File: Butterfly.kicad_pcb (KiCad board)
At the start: 2 copper layers, 93.1 x 65.5 mm, 28 parts, among them J1 Conn_02x03_Odd_Even, J2 USB_A, U1 ATTINY85-20PU

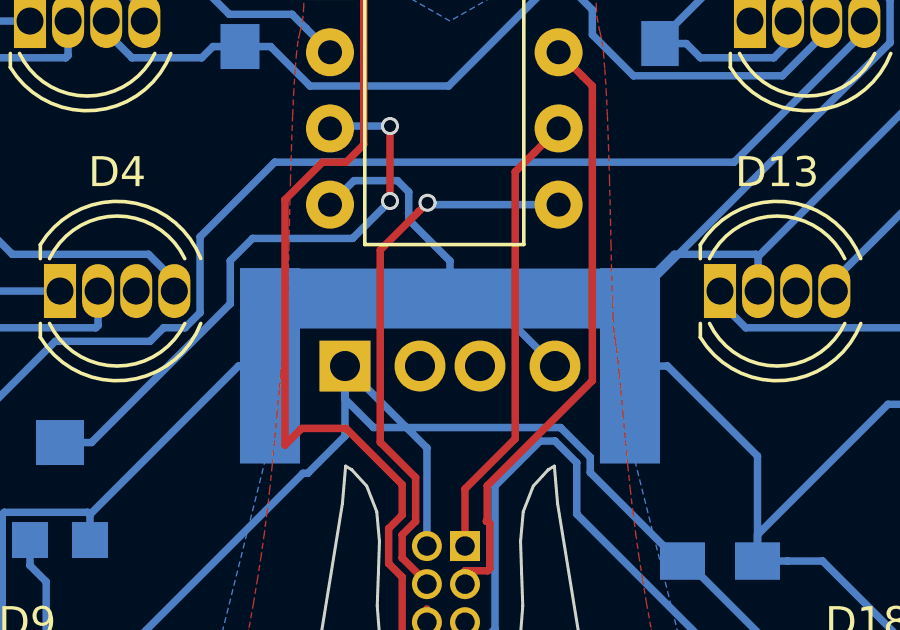
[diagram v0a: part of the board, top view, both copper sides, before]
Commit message: Fill zones.
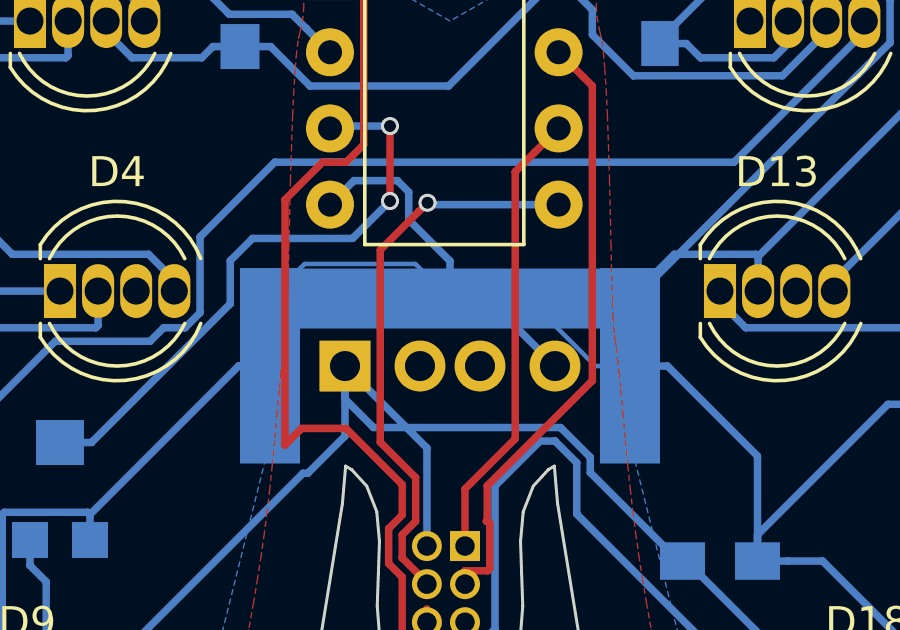
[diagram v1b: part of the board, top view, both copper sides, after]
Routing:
- net GND: track 407.0 -> 423.2 mm
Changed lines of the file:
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@@
   (general
     (links 75)
-    (no_connects 16)
+    (no_connects 0)
     (area 98.409153 69.322099 191.590847 134.925641)
     (thickness 1.6)
     (drawings 182)
-    (tracks 337)
+    (tracks 344)
     (zones 0)
     (modules 28)
@@
   (segment (start 152 93.25) (end 148.87 93.25) (width 0.25) (layer B.Cu) (net 1))
   (segment (start 148.87 93.25) (end 148.62 93.5) (width 0.25) (layer B.Cu) (net 1))
+  (segment (start 145 104.25) (end 147.5976 104.25) (width 0.1524) (layer B.Cu) (net 2))
+  (segment (start 147.5976 104.25) (end 149.8476 106.5) (width 0.1524) (layer B.Cu) (net 2))
+  (segment (start 149.8476 106.5) (end 151 106.5) (width 0.1524) (layer B.Cu) (net 2))
+  (segment (start 139 106.5) (end 139 104.25) (width 0.1524) (layer B.Cu) (net 2))
+  (segment (start 139 104.25) (end 140.1524 103.0976) (width 0.1524) (layer B.Cu) (net 2))
+  (segment (start 143.8476 103.0976) (end 145 104.25) (width 0.1524) (layer B.Cu) (net 2))
+  (segment (start 140.1524 103.0976) (end 143.8476 103.0976) (width 0.1524) (layer B.Cu) (net 2))
   (segment (start 130.27 119) (end 130.27 117.85) (width 0.25) (layer B.Cu) (net 2))
   (segment (start 130.27 117.85) (end 130.074999 117.654999) (width 0.25) (layer B.Cu) (net 2))
@@
     (connect_pads (clearance 0.508))
     (min_thickness 0.254)
-    (fill (arc_segments 16) (thermal_gap 0.508) (thermal_bridge_width 0.508))
+    (fill yes (arc_segments 16) (thermal_gap 0.508) (thermal_bridge_width 0.508))
     (polygon
       (pts
@@
         (xy 101.159481 75.389431) (xy 101.268235 74.91297) (xy 101.448595 74.425842) (xy 101.611785 74.073037) (xy 102.058151 73.335693)
         (xy 102.610262 72.72205) (xy 103.258173 72.24239) (xy 103.51812 72.10195) (xy 103.815052 71.962921) (xy 104.052406 71.87908)
-        (xy 104.292884 71.837641) (xy 104.599189 71.825822) (xy 104.86207 71.82795)
+        (xy 104.292884 71.837641) (xy 104.599189 71.825822)
       )
     )
@@
     (connect_pads (clearance 0.508))
     (min_thickness 0.254)
-    (fill (arc_segments 16) (thermal_gap 0.508) (thermal_bridge_width 0.508))
+    (fill yes (arc_segments 16) (thermal_gap 0.508) (thermal_bridge_width 0.508))
     (polygon
       (pts
@@
         (xy 188.840519 75.389431) (xy 188.731765 74.91297) (xy 188.551405 74.425842) (xy 188.388215 74.073037) (xy 187.941849 73.335693)
         (xy 187.389738 72.72205) (xy 186.741827 72.24239) (xy 186.48188 72.10195) (xy 186.184948 71.962921) (xy 185.947594 71.87908)
-        (xy 185.707116 71.837641) (xy 185.400811 71.825822) (xy 185.13793 71.82795)
+        (xy 185.707116 71.837641) (xy 185.400811 71.825822)
       )
     )
@@
     (connect_pads (clearance 0.508))
     (min_thickness 0.254)
-    (fill (arc_segments 16) (thermal_gap 0.508) (thermal_bridge_width 0.508))
+    (fill yes (arc_segments 16) (thermal_gap 0.508) (thermal_bridge_width 0.508))
     (polygon
       (pts
         (xy 145 95) (xy 110 75) (xy 105 90) (xy 120 105) (xy 120 125)
         (xy 135 125) (xy 140 105) (xy 150 105) (xy 155 125) (xy 170 125)
-        (xy 170 105) (xy 185 90) (xy 180 75) (xy 145 95)
+        (xy 170 105) (xy 185 90) (xy 180 75)
       )
     )

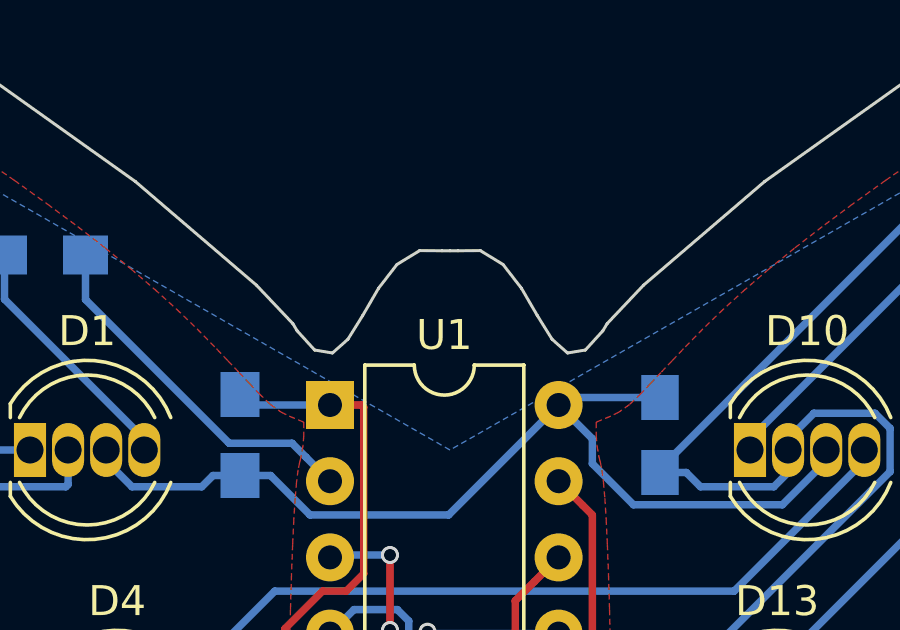
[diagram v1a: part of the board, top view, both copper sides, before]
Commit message: Add antenna holes.
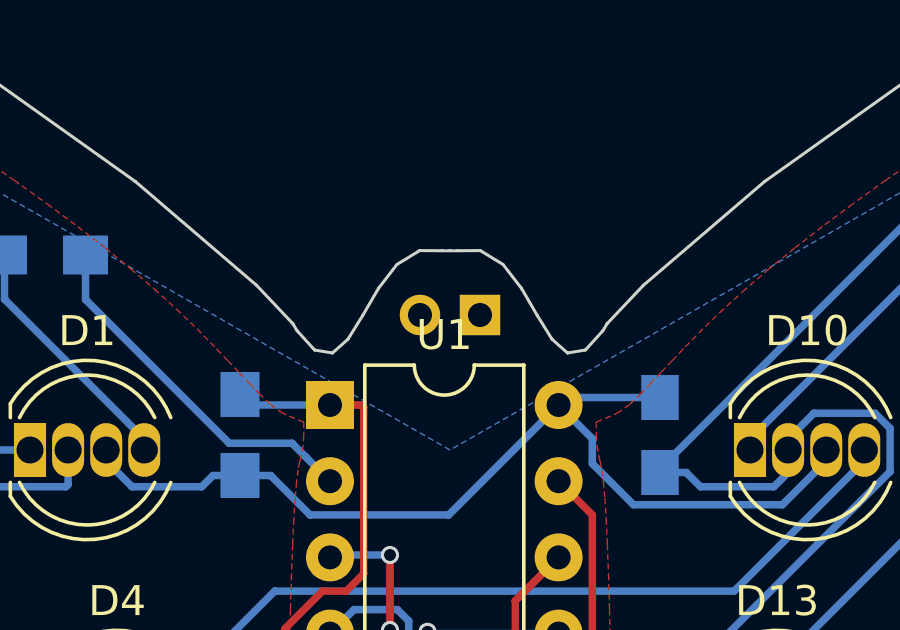
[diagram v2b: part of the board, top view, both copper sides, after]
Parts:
- added J3: Conn_01x02, Pin_Headers:Pin_Header_Straight_1x02_Pitch2.00mm, B.Cu at (146.0, 90.5)
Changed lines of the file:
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@@
 (kicad_pcb (version 4) (host pcbnew 4.0.7)
   (general
-    (links 75)
-    (no_connects 0)
-    (area 98.409153 69.322099 191.590847 134.925641)
+    (links 76)
+    (no_connects 1)
+    (area 98.409153 69.322099 191.590847 150.013041)
     (thickness 1.6)
     (drawings 182)
     (tracks 344)
     (zones 0)
-    (modules 28)
-    (nets 30)
+    (modules 29)
+    (nets 31)
   )
   (page USLetter)
@@
   (net 28 "Net-(R1-Pad2)")
   (net 29 "Net-(POT1-Pad2)")
+  (net 30 "Net-(J3-Pad1)")
   (net_class Default "This is the default net class."
     (clearance 0.1524)
@@
     (add_net "Net-(J2-Pad2)")
     (add_net "Net-(J2-Pad3)")
+    (add_net "Net-(J3-Pad1)")
     (add_net "Net-(POT1-Pad2)")
     (add_net "Net-(R1-Pad2)")
@@
       (net 1 +5V))
   )
+  (module Pin_Headers:Pin_Header_Straight_1x02_Pitch2.00mm (layer B.Cu)
+    (at 146 90.5 90)
+    (descr "Through hole straight pin header, 1x02, 2.00mm pitch, single row")
+    (tags "Through hole pin header THT 1x02 2.00mm single row")
+    (fp_text reference J3 (at 0 2.06 90) (layer B.SilkS) hide
+      (effects (font (size 1 1) (thickness 0.15)) (justify mirror))
+    )
+    (fp_text value Conn_01x02 (at 0 -4.06 90) (layer B.Fab)
+      (effects (font (size 1 1) (thickness 0.15)) (justify mirror))
+    )
+    (fp_line (start -0.5 1) (end 1 1) (layer B.Fab) (width 0.1))
+    (fp_line (start 1 1) (end 1 -3) (layer B.Fab) (width 0.1))
+    (fp_line (start 1 -3) (end -1 -3) (layer B.Fab) (width 0.1))
+    (fp_line (start -1 -3) (end -1 0.5) (layer B.Fab) (width 0.1))
+    (fp_line (start -1 0.5) (end -0.5 1) (layer B.Fab) (width 0.1))
+    (fp_line (start -1.06 -3.06) (end 1.06 -3.06) (layer B.SilkS) (width 0.12))
+    (fp_line (start -1.06 -1) (end -1.06 -3.06) (layer B.SilkS) (width 0.12))
+    (fp_line (start 1.06 -1) (end 1.06 -3.06) (layer B.SilkS) (width 0.12))
+    (fp_line (start -1.06 -1) (end 1.06 -1) (layer B.SilkS) (width 0.12))
+    (fp_line (start -1.06 0) (end -1.06 1.06) (layer B.SilkS) (width 0.12))
+    (fp_line (start -1.06 1.06) (end 0 1.06) (layer B.SilkS) (width 0.12))
+    (fp_line (start -1.5 1.5) (end -1.5 -3.5) (layer B.CrtYd) (width 0.05))
+    (fp_line (start -1.5 -3.5) (end 1.5 -3.5) (layer B.CrtYd) (width 0.05))
+    (fp_line (start 1.5 -3.5) (end 1.5 1.5) (layer B.CrtYd) (width 0.05))
+    (fp_line (start 1.5 1.5) (end -1.5 1.5) (layer B.CrtYd) (width 0.05))
+    (fp_text user %R (at 0 -1 360) (layer B.Fab)
+      (effects (font (size 1 1) (thickness 0.15)) (justify mirror))
+    )
+    (pad 1 thru_hole rect (at 0 0 90) (size 1.35 1.35) (drill 0.8) (layers *.Cu *.Mask)
+      (net 30 "Net-(J3-Pad1)"))
+    (pad 2 thru_hole oval (at 0 -2 90) (size 1.35 1.35) (drill 0.8) (layers *.Cu *.Mask)
+      (net 30 "Net-(J3-Pad1)"))
+    (model ${KISYS3DMOD}/Pin_Headers.3dshapes/Pin_Header_Straight_1x02_Pitch2.00mm.wrl
+      (at (xyz 0 0 0))
+      (scale (xyz 1 1 1))
+      (rotate (xyz 0 0 0))
+    )
+  )
   (gr_line (start 143.98953 88.3529) (end 143.23173 88.8161) (layer Edge.Cuts) (width 0.1))

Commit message: Set solder mask clearance to 0.
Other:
- rule pad_to_mask_clearance: 0.2 -> 0
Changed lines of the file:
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@@
     (pad_size 1.524 1.524)
     (pad_drill 0.762)
-    (pad_to_mask_clearance 0.2)
+    (pad_to_mask_clearance 0)
     (aux_axis_origin 0 0)
     (visible_elements FFFEF77F)
